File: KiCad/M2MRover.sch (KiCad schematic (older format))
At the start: 31 parts, among them J1 Light Detection, J10 MPU6050 Gyro & Acc GY-521, J11 microbit_edge_connector, J2 Serial (Bluetooth), J3 Servo, J4 H-Bridge, J5 Ultrasonic Down, J6 Ultrasonic Forward, J7 Compass GY-273, J8 Left Hall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

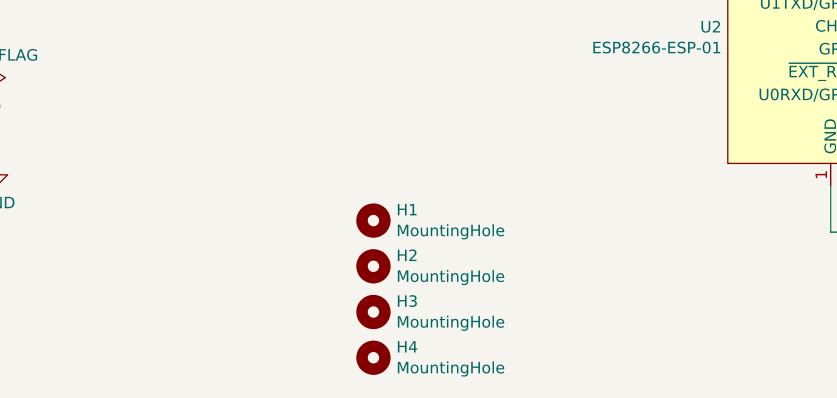
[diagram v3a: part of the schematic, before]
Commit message: Add initial PCB layout
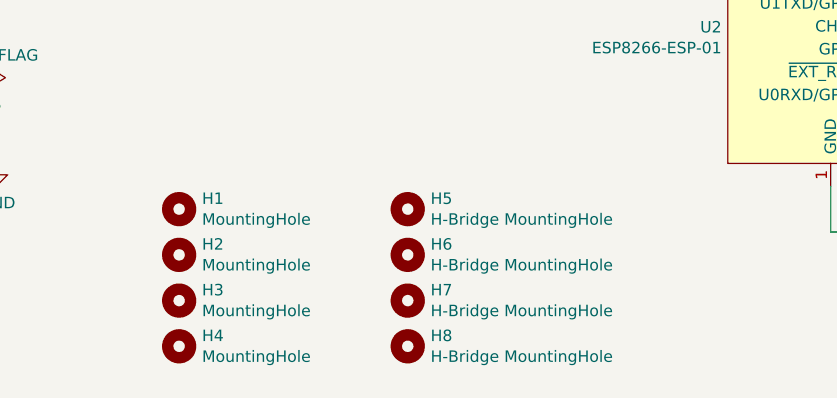
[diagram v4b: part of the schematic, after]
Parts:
- added H5, H6, H7, H8: H-Bridge MountingHole, MountingHole:MountingHole_2.7mm_Pad, symbol Mechanical:MountingHole
- H1, H2, H3, H4: footprint MountingHole:MountingHole_4.3mm_M4_Pad -> MountingHole:MountingHole_2.7mm_Pad
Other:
- moved on the sheet: H1, H2, H3, H4
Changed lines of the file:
@@
 L Mechanical:MountingHole H1
 U 1 1 5D604FCC
-P 3350 7050
-F 0 "H1" H 3450 7096 50  0000 L CNN
-F 1 "MountingHole" H 3450 7005 50  0000 L CNN
-F 2 "MountingHole:MountingHole_4.3mm_M4_Pad" H 3350 7050 50  0001 C CNN
-F 3 "~" H 3350 7050 50  0001 C CNN
-	1    3350 7050
+P 2500 7000
+F 0 "H1" H 2600 7046 50  0000 L CNN
+F 1 "MountingHole" H 2600 6955 50  0000 L CNN
+F 2 "MountingHole:MountingHole_2.7mm_Pad" H 2500 7000 50  0001 C CNN
+F 3 "~" H 2500 7000 50  0001 C CNN
+	1    2500 7000
 	1    0    0    -1
 $EndComp
@@
 L Mechanical:MountingHole H2
 U 1 1 5D605AC0
-P 3350 7250
-F 0 "H2" H 3450 7296 50  0000 L CNN
-F 1 "MountingHole" H 3450 7205 50  0000 L CNN
-F 2 "MountingHole:MountingHole_4.3mm_M4_Pad" H 3350 7250 50  0001 C CNN
-F 3 "~" H 3350 7250 50  0001 C CNN
-	1    3350 7250
+P 2500 7200
+F 0 "H2" H 2600 7246 50  0000 L CNN
+F 1 "MountingHole" H 2600 7155 50  0000 L CNN
+F 2 "MountingHole:MountingHole_2.7mm_Pad" H 2500 7200 50  0001 C CNN
+F 3 "~" H 2500 7200 50  0001 C CNN
+	1    2500 7200
 	1    0    0    -1
 $EndComp
@@
 L Mechanical:MountingHole H3
 U 1 1 5D606344
-P 3350 7450
-F 0 "H3" H 3450 7496 50  0000 L CNN
-F 1 "MountingHole" H 3450 7405 50  0000 L CNN
-F 2 "MountingHole:MountingHole_4.3mm_M4_Pad" H 3350 7450 50  0001 C CNN
-F 3 "~" H 3350 7450 50  0001 C CNN
-	1    3350 7450
+P 2500 7400
+F 0 "H3" H 2600 7446 50  0000 L CNN
+F 1 "MountingHole" H 2600 7355 50  0000 L CNN
+F 2 "MountingHole:MountingHole_2.7mm_Pad" H 2500 7400 50  0001 C CNN
+F 3 "~" H 2500 7400 50  0001 C CNN
+	1    2500 7400
 	1    0    0    -1
 $EndComp
@@
 L Mechanical:MountingHole H4
 U 1 1 5D606BD0
-P 3350 7650
-F 0 "H4" H 3450 7696 50  0000 L CNN
-F 1 "MountingHole" H 3450 7605 50  0000 L CNN
-F 2 "MountingHole:MountingHole_4.3mm_M4_Pad" H 3350 7650 50  0001 C CNN
-F 3 "~" H 3350 7650 50  0001 C CNN
-	1    3350 7650
+P 2500 7600
+F 0 "H4" H 2600 7646 50  0000 L CNN
+F 1 "MountingHole" H 2600 7555 50  0000 L CNN
+F 2 "MountingHole:MountingHole_2.7mm_Pad" H 2500 7600 50  0001 C CNN
+F 3 "~" H 2500 7600 50  0001 C CNN
+	1    2500 7600
 	1    0    0    -1
 $EndComp
@@
 Wire Wire Line
 	6850 800  6850 950
+$Comp
+L Mechanical:MountingHole H5
+U 1 1 5D6E129D
+P 3500 7000
+F 0 "H5" H 3600 7046 50  0000 L CNN
+F 1 "H-Bridge MountingHole" H 3600 6955 50  0000 L CNN
+F 2 "MountingHole:MountingHole_2.7mm_Pad" H 3500 7000 50  0001 C CNN
+F 3 "~" H 3500 7000 50  0001 C CNN
+	1    3500 7000
+	1    0    0    -1
+$EndComp
+$Comp
+L Mechanical:MountingHole H6
+U 1 1 5D6E24EF
+P 3500 7200
+F 0 "H6" H 3600 7246 50  0000 L CNN
+F 1 "H-Bridge MountingHole" H 3600 7155 50  0000 L CNN
+F 2 "MountingHole:MountingHole_2.7mm_Pad" H 3500 7200 50  0001 C CNN
+F 3 "~" H 3500 7200 50  0001 C CNN
+	1    3500 7200
+	1    0    0    -1
+$EndComp
+$Comp
+L Mechanical:MountingHole H7
+U 1 1 5D6E29B7
+P 3500 7400
+F 0 "H7" H 3600 7446 50  0000 L CNN
+F 1 "H-Bridge MountingHole" H 3600 7355 50  0000 L CNN
+F 2 "MountingHole:MountingHole_2.7mm_Pad" H 3500 7400 50  0001 C CNN
+F 3 "~" H 3500 7400 50  0001 C CNN
+	1    3500 7400
+	1    0    0    -1
+$EndComp
+$Comp
+L Mechanical:MountingHole H8
+U 1 1 5D6E2E93
+P 3500 7600
+F 0 "H8" H 3600 7646 50  0000 L CNN
+F 1 "H-Bridge MountingHole" H 3600 7555 50  0000 L CNN
+F 2 "MountingHole:MountingHole_2.7mm_Pad" H 3500 7600 50  0001 C CNN
+F 3 "~" H 3500 7600 50  0001 C CNN
+	1    3500 7600
+	1    0    0    -1
+$EndComp
 $EndSCHEMATC

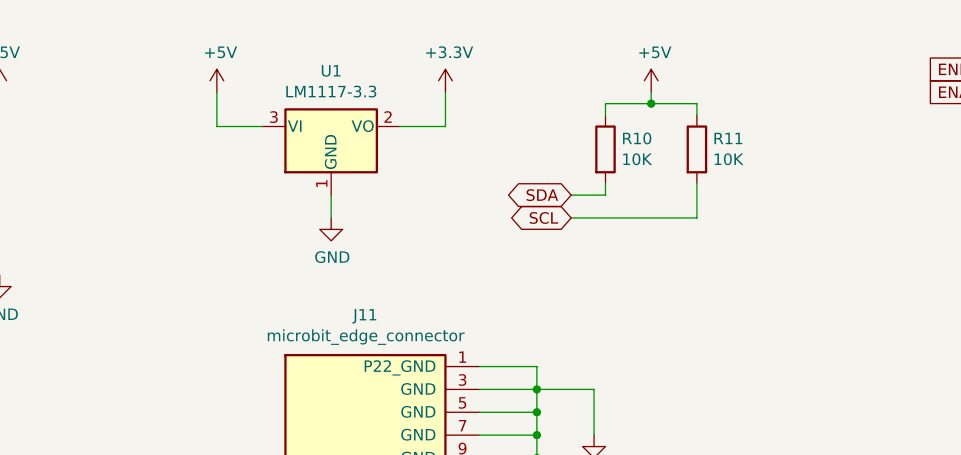
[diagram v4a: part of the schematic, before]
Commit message: Change 3.3V regulator to LD1117
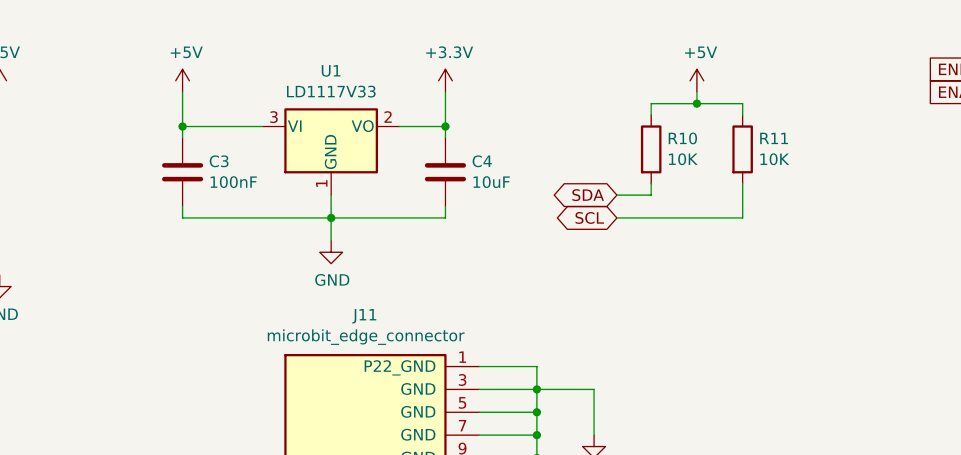
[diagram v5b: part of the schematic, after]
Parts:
- removed U1: LM1117-3.3, Package_TO_SOT_THT:TO-220-3_Vertical, symbol Regulator_Linear:LM1117-3.3
- added C3: 100nF, symbol Device:C
- added C4: 10uF, symbol Device:C
- added U1: LD1117V33, Package_TO_SOT_THT:TO-220-3_Vertical, symbol Regulator_Linear:LD1117S33TR_SOT223
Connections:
- net +3V3: now also C4.1, U1.2 (VO)
- net +5V: now also C3.1, U1.3 (VI)
- net GND: now also C3.2, C4.2, U1.1 (GND)
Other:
- moved on the sheet: R10, R11

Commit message: Add footprints for passive components
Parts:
- C1, C2, C3, C4: footprint (none) -> Capacitor_SMD:C_0805_2012Metric_Pad1.15x1.40mm_HandSolder
- R1, R10, R11, R2, R3, R4, R5, R6, R7, R8, R9: footprint (none) -> Resistor_SMD:R_0805_2012Metric_Pad1.15x1.40mm_HandSolder
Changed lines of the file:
@@
 F 0 "R1" H 1470 2846 50  0000 L CNN
 F 1 "10K" H 1470 2755 50  0000 L CNN
-F 2 "" V 1330 2800 50  0001 C CNN
+F 2 "Resistor_SMD:R_0805_2012Metric_Pad1.15x1.40mm_HandSolder" V 1330 2800 50  0001 C CNN
 F 3 "~" H 1400 2800 50  0001 C CNN
 	1    1400 2800
@@
 F 0 "R2" H 1770 2846 50  0000 L CNN
 F 1 "10K" H 1770 2755 50  0000 L CNN
-F 2 "" V 1630 2800 50  0001 C CNN
+F 2 "Resistor_SMD:R_0805_2012Metric_Pad1.15x1.40mm_HandSolder" V 1630 2800 50  0001 C CNN
 F 3 "~" H 1700 2800 50  0001 C CNN
 	1    1700 2800
@@
 F 0 "R3" H 2070 2846 50  0000 L CNN
 F 1 "10K" H 2070 2755 50  0000 L CNN
-F 2 "" V 1930 2800 50  0001 C CNN
+F 2 "Resistor_SMD:R_0805_2012Metric_Pad1.15x1.40mm_HandSolder" V 1930 2800 50  0001 C CNN
 F 3 "~" H 2000 2800 50  0001 C CNN
 	1    2000 2800
@@
 F 0 "R4" H 10070 5096 50  0000 L CNN
 F 1 "10K" H 10070 5005 50  0000 L CNN
-F 2 "" V 9930 5050 50  0001 C CNN
+F 2 "Resistor_SMD:R_0805_2012Metric_Pad1.15x1.40mm_HandSolder" V 9930 5050 50  0001 C CNN
 F 3 "~" H 10000 5050 50  0001 C CNN
 	1    10000 5050
@@
 F 0 "R5" H 10370 5096 50  0000 L CNN
 F 1 "10K" H 10370 5005 50  0000 L CNN
-F 2 "" V 10230 5050 50  0001 C CNN
+F 2 "Resistor_SMD:R_0805_2012Metric_Pad1.15x1.40mm_HandSolder" V 10230 5050 50  0001 C CNN
 F 3 "~" H 10300 5050 50  0001 C CNN
 	1    10300 5050
@@
 F 0 "R9" H 6420 6296 50  0000 L CNN
 F 1 "10K" H 6420 6205 50  0000 L CNN
-F 2 "" V 6280 6250 50  0001 C CNN
+F 2 "Resistor_SMD:R_0805_2012Metric_Pad1.15x1.40mm_HandSolder" V 6280 6250 50  0001 C CNN
 F 3 "~" H 6350 6250 50  0001 C CNN
 	1    6350 6250
@@
 F 0 "R8" H 6170 5946 50  0000 L CNN
 F 1 "10K" H 6170 5855 50  0000 L CNN
-F 2 "" V 6030 5900 50  0001 C CNN
+F 2 "Resistor_SMD:R_0805_2012Metric_Pad1.15x1.40mm_HandSolder" V 6030 5900 50  0001 C CNN
 F 3 "~" H 6100 5900 50  0001 C CNN
 	1    6100 5900
@@
 F 0 "R6" H 6770 6246 50  0000 L CNN
 F 1 "1K" H 6770 6155 50  0000 L CNN
-F 2 "" V 6630 6200 50  0001 C CNN
+F 2 "Resistor_SMD:R_0805_2012Metric_Pad1.15x1.40mm_HandSolder" V 6630 6200 50  0001 C CNN
 F 3 "~" H 6700 6200 50  0001 C CNN
 	1    6700 6200
@@
 F 0 "R7" H 6770 6896 50  0000 L CNN
 F 1 "2K" H 6770 6805 50  0000 L CNN
-F 2 "" V 6630 6850 50  0001 C CNN
+F 2 "Resistor_SMD:R_0805_2012Metric_Pad1.15x1.40mm_HandSolder" V 6630 6850 50  0001 C CNN
 F 3 "~" H 6700 6850 50  0001 C CNN
 	1    6700 6850
@@
 F 0 "R10" H 4820 1196 50  0000 L CNN
 F 1 "10K" H 4820 1105 50  0000 L CNN
-F 2 "" V 4680 1150 50  0001 C CNN
+F 2 "Resistor_SMD:R_0805_2012Metric_Pad1.15x1.40mm_HandSolder" V 4680 1150 50  0001 C CNN
 F 3 "~" H 4750 1150 50  0001 C CNN
 	1    4750 1150
@@
 F 0 "R11" H 5220 1196 50  0000 L CNN
 F 1 "10K" H 5220 1105 50  0000 L CNN
-F 2 "" V 5080 1150 50  0001 C CNN
+F 2 "Resistor_SMD:R_0805_2012Metric_Pad1.15x1.40mm_HandSolder" V 5080 1150 50  0001 C CNN
 F 3 "~" H 5150 1150 50  0001 C CNN
 	1    5150 1150
@@
 F 0 "C1" H 6465 1146 50  0000 L CNN
 F 1 "10pF" H 6465 1055 50  0000 L CNN
-F 2 "" H 6388 950 50  0001 C CNN
+F 2 "Capacitor_SMD:C_0805_2012Metric_Pad1.15x1.40mm_HandSolder" H 6388 950 50  0001 C CNN
 F 3 "~" H 6350 1100 50  0001 C CNN
 	1    6350 1100
@@
 F 0 "C2" H 6965 1146 50  0000 L CNN
 F 1 "10pF" H 6965 1055 50  0000 L CNN
-F 2 "" H 6888 950 50  0001 C CNN
+F 2 "Capacitor_SMD:C_0805_2012Metric_Pad1.15x1.40mm_HandSolder" H 6888 950 50  0001 C CNN
 F 3 "~" H 6850 1100 50  0001 C CNN
 	1    6850 1100
@@
 F 0 "C4" H 3965 1296 50  0000 L CNN
 F 1 "10uF" H 3965 1205 50  0000 L CNN
-F 2 "" H 3888 1100 50  0001 C CNN
+F 2 "Capacitor_SMD:C_0805_2012Metric_Pad1.15x1.40mm_HandSolder" H 3888 1100 50  0001 C CNN
 F 3 "~" H 3850 1250 50  0001 C CNN
 	1    3850 1250
@@
 F 0 "C3" H 2815 1296 50  0000 L CNN
 F 1 "100nF" H 2815 1205 50  0000 L CNN
-F 2 "" H 2738 1100 50  0001 C CNN
+F 2 "Capacitor_SMD:C_0805_2012Metric_Pad1.15x1.40mm_HandSolder" H 2738 1100 50  0001 C CNN
 F 3 "~" H 2700 1250 50  0001 C CNN
 	1    2700 1250

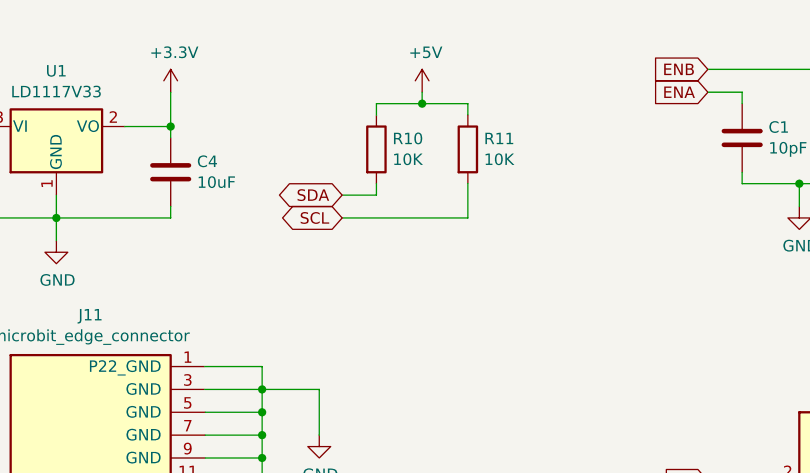
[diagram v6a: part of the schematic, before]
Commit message: Add jumpers to I2C lines and start PCB layout
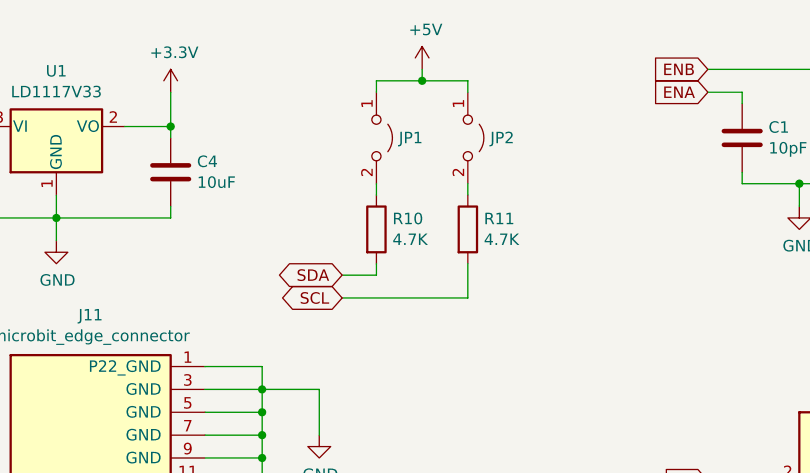
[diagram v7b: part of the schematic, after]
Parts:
- added JP1, JP2: Jumper_2_Open, Connector_PinHeader_2.54mm:PinHeader_1x02_P2.54mm_Vertical, symbol Jumper:Jumper_2_Open
- R10, R11: value 10K -> 4.7K
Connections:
- net +5V: now also JP1.1 (A), JP2.1 (A); no longer R10.1, R11.1
- new net: JP1.2 (B), R10.1
- new net: JP2.2 (B), R11.1
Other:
- moved on the sheet: R10, R11
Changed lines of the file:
@@
 Wire Wire Line
 	6100 6200 6100 6050
-Text GLabel 4600 1350 0    50   BiDi ~ 0
+Text GLabel 4600 1700 0    50   BiDi ~ 0
 SDA
-Text GLabel 4600 1450 0    50   BiDi ~ 0
+Text GLabel 4600 1800 0    50   BiDi ~ 0
 SCL
 $Comp
 L Device:R R10
 U 1 1 5D68795D
-P 4750 1150
-F 0 "R10" H 4820 1196 50  0000 L CNN
-F 1 "10K" H 4820 1105 50  0000 L CNN
-F 2 "Resistor_SMD:R_0805_2012Metric_Pad1.15x1.40mm_HandSolder" V 4680 1150 50  0001 C CNN
-F 3 "~" H 4750 1150 50  0001 C CNN
-	1    4750 1150
+P 4750 1500
+F 0 "R10" H 4820 1546 50  0000 L CNN
+F 1 "4.7K" H 4820 1455 50  0000 L CNN
+F 2 "Resistor_SMD:R_0805_2012Metric_Pad1.15x1.40mm_HandSolder" V 4680 1500 50  0001 C CNN
+F 3 "~" H 4750 1500 50  0001 C CNN
+	1    4750 1500
 	1    0    0    -1
 $EndComp
@@
 L Device:R R11
 U 1 1 5D6882C9
-P 5150 1150
-F 0 "R11" H 5220 1196 50  0000 L CNN
-F 1 "10K" H 5220 1105 50  0000 L CNN
-F 2 "Resistor_SMD:R_0805_2012Metric_Pad1.15x1.40mm_HandSolder" V 5080 1150 50  0001 C CNN
-F 3 "~" H 5150 1150 50  0001 C CNN
-	1    5150 1150
+P 5150 1500
+F 0 "R11" H 5220 1546 50  0000 L CNN
+F 1 "4.7K" H 5220 1455 50  0000 L CNN
+F 2 "Resistor_SMD:R_0805_2012Metric_Pad1.15x1.40mm_HandSolder" V 5080 1500 50  0001 C CNN
+F 3 "~" H 5150 1500 50  0001 C CNN
+	1    5150 1500
 	1    0    0    -1
 $EndComp
@@
 L power:+5V #PWR0116
 U 1 1 5D688A7F
-P 4950 900
-F 0 "#PWR0116" H 4950 750 50  0001 C CNN
-F 1 "+5V" H 4965 1073 50  0000 C CNN
-F 2 "" H 4950 900 50  0001 C CNN
-F 3 "" H 4950 900 50  0001 C CNN
-	1    4950 900
-	1    0    0    -1
-$EndComp
-Wire Wire Line
-	4600 1350 4750 1350
-Wire Wire Line
-	4750 1350 4750 1300
-Wire Wire Line
-	4600 1450 5150 1450
-Wire Wire Line
-	5150 1450 5150 1300
-Wire Wire Line
-	4750 1000 4750 950
-Wire Wire Line
-	4750 950  4950 950
-Wire Wire Line
-	5150 950  5150 1000
-Wire Wire Line
-	4950 900  4950 950
-Connection ~ 4950 950
-Wire Wire Line
-	4950 950  5150 950
+P 4950 800
+F 0 "#PWR0116" H 4950 650 50  0001 C CNN
+F 1 "+5V" H 4965 973 50  0000 C CNN
+F 2 "" H 4950 800 50  0001 C CNN
+F 3 "" H 4950 800 50  0001 C CNN
+	1    4950 800
+	1    0    0    -1
+$EndComp
+Wire Wire Line
+	4600 1700 4750 1700
+Wire Wire Line
+	4750 1700 4750 1650
+Wire Wire Line
+	4600 1800 5150 1800
+Wire Wire Line
+	5150 1800 5150 1650
+Wire Wire Line
+	4750 900  4750 850
+Wire Wire Line
+	4750 850  4950 850
+Wire Wire Line
+	5150 850  5150 900
+Wire Wire Line
+	4950 800  4950 850
+Connection ~ 4950 850
+Wire Wire Line
+	4950 850  5150 850
 $Comp
 L power:GND #PWR0117
@@
 Connection ~ 2700 1050
 Connection ~ 3850 1050
+$Comp
+L Jumper:Jumper_2_Open JP1
+U 1 1 5D714150
+P 4750 1100
+F 0 "JP1" V 4750 1198 50  0000 L CNN
+F 1 "Jumper_2_Open" V 4795 1198 50  0001 L CNN
+F 2 "Connector_PinHeader_2.54mm:PinHeader_1x02_P2.54mm_Vertical" H 4750 1100 50  0001 C CNN
+F 3 "~" H 4750 1100 50  0001 C CNN
+	1    4750 1100
+	0    1    1    0
+$EndComp
+$Comp
+L Jumper:Jumper_2_Open JP2
+U 1 1 5D716FA0
+P 5150 1100
+F 0 "JP2" V 5150 1198 50  0000 L CNN
+F 1 "Jumper_2_Open" V 5195 1198 50  0001 L CNN
+F 2 "Connector_PinHeader_2.54mm:PinHeader_1x02_P2.54mm_Vertical" H 5150 1100 50  0001 C CNN
+F 3 "~" H 5150 1100 50  0001 C CNN
+	1    5150 1100
+	0    1    1    0
+$EndComp
+Wire Wire Line
+	4750 1300 4750 1350
+Wire Wire Line
+	5150 1300 5150 1350
 $EndSCHEMATC
